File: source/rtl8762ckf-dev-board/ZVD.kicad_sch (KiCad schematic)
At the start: 4 parts, among them Q1 BC807DS,115, Q2 AO3401A

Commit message: implemented pico probe
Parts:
- Q1: footprint Package_SO:SC-74-6_1.5x2.9mm_P0.95mm -> Package_TO_SOT_SMD:SOT-363_SC-70-6; LCSC (none) -> C2836075; MPN (none) -> MMDT3906DW K3N
- Q2: LCSC (none) -> C15127; MPN (none) -> AO3401A
- R10: LCSC (none) -> C25792; MPN (none) -> 0402WGF4702TCE
- R9: LCSC (none) -> C25086; MPN (none) -> 0402WGF100KTCE
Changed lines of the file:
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@@
       (effects (font (size 1.27 1.27)) (justify left))
     )
-    (property "Footprint" "Package_SO:SC-74-6_1.5x2.9mm_P0.95mm" (at 48.26 58.42 0)
-      (effects (font (size 1.27 1.27)) hide)
-    )
-    (property "Datasheet" "http://www.diodes.com/_files/datasheets/ds30125.pdf" (at 53.34 60.96 0)
+    (property "Footprint" "Package_TO_SOT_SMD:SOT-363_SC-70-6" (at 48.26 58.42 0)
+      (effects (font (size 1.27 1.27)) hide)
+    )
+    (property "Datasheet" "https://datasheet.lcsc.com/lcsc/2202131900_CBI-MMDT3906DW-K3N_C2836075.pdf" (at 53.34 60.96 0)
+      (effects (font (size 1.27 1.27)) hide)
+    )
+    (property "LCSC" "C2836075" (at 53.34 60.96 0)
+      (effects (font (size 1.27 1.27)) hide)
+    )
+    (property "MPN" "MMDT3906DW K3N" (at 53.34 60.96 0)
       (effects (font (size 1.27 1.27)) hide)
     )
@@
       (effects (font (size 1.27 1.27)) (justify left) hide)
     )
+    (property "LCSC" "C15127" (at 63.5 53.34 0)
+      (effects (font (size 1.27 1.27)) hide)
+    )
+    (property "MPN" "AO3401A" (at 63.5 53.34 0)
+      (effects (font (size 1.27 1.27)) hide)
+    )
     (pin "1")
     (pin "2")
@@
       (project "rtl8762ckf-dev-board"
         (path "/5477044b-5ae5-4ed6-bb7d-f5f3cc95a2d4/c23b56eb-ac59-4603-b11b-f6fc1d31d5c9"
-          (reference "#PWR014") (unit 1)
+          (reference "#PWR031") (unit 1)
         )
       )
@@
       (project "rtl8762ckf-dev-board"
         (path "/5477044b-5ae5-4ed6-bb7d-f5f3cc95a2d4/c23b56eb-ac59-4603-b11b-f6fc1d31d5c9"
-          (reference "#PWR015") (unit 1)
+          (reference "#PWR032") (unit 1)
         )
       )
@@
       (effects (font (size 1.27 1.27)) hide)
     )
+    (property "LCSC" "C25792" (at 76.2 73.66 0)
+      (effects (font (size 1.27 1.27)) hide)
+    )
+    (property "MPN" "0402WGF4702TCE" (at 76.2 73.66 0)
+      (effects (font (size 1.27 1.27)) hide)
+    )
     (pin "1")
     (pin "2")
@@
       (project "rtl8762ckf-dev-board"
         (path "/5477044b-5ae5-4ed6-bb7d-f5f3cc95a2d4/c23b56eb-ac59-4603-b11b-f6fc1d31d5c9"
-          (reference "R5") (unit 1)
+          (reference "R9") (unit 1)
         )
       )
@@
       (effects (font (size 1.27 1.27)) (justify left))
     )
-    (property "Footprint" "Package_SO:SC-74-6_1.5x2.9mm_P0.95mm" (at 78.74 58.42 0)
-      (effects (font (size 1.27 1.27)) hide)
-    )
-    (property "Datasheet" "http://www.diodes.com/_files/datasheets/ds30125.pdf" (at 73.66 60.96 0)
+    (property "Footprint" "Package_TO_SOT_SMD:SOT-363_SC-70-6" (at 78.74 58.42 0)
+      (effects (font (size 1.27 1.27)) hide)
+    )
+    (property "Datasheet" "https://datasheet.lcsc.com/lcsc/2202131900_CBI-MMDT3906DW-K3N_C2836075.pdf" (at 73.66 60.96 0)
+      (effects (font (size 1.27 1.27)) hide)
+    )
+    (property "LCSC" "C2836075" (at 73.66 60.96 0)
+      (effects (font (size 1.27 1.27)) hide)
+    )
+    (property "MPN" "MMDT3906DW K3N" (at 73.66 60.96 0)
       (effects (font (size 1.27 1.27)) hide)
     )
@@
       (effects (font (size 1.27 1.27)) hide)
     )
-    (property "Datasheet" "~" (at 50.8 73.66 0)
+    (property "Datasheet" "https://datasheet.lcsc.com/lcsc/2205311900_UNI-ROYAL-Uniroyal-Elec-0402WGF100KTCE_C25086.pdf" (at 50.8 73.66 0)
+      (effects (font (size 1.27 1.27)) hide)
+    )
+    (property "LCSC" "C25086" (at 50.8 73.66 0)
+      (effects (font (size 1.27 1.27)) hide)
+    )
+    (property "MPN" "0402WGF100KTCE" (at 50.8 73.66 0)
       (effects (font (size 1.27 1.27)) hide)
     )
@@
       (project "rtl8762ckf-dev-board"
         (path "/5477044b-5ae5-4ed6-bb7d-f5f3cc95a2d4/c23b56eb-ac59-4603-b11b-f6fc1d31d5c9"
-          (reference "R4") (unit 1)
-        )
-      )
+          (reference "R8") (unit 1)
+        )
+      )

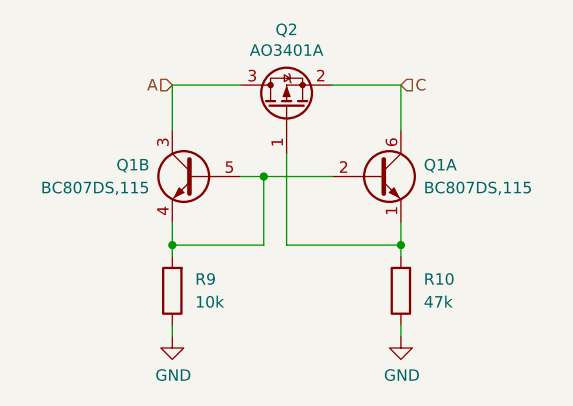
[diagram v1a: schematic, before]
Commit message: correct zvd; closes #4
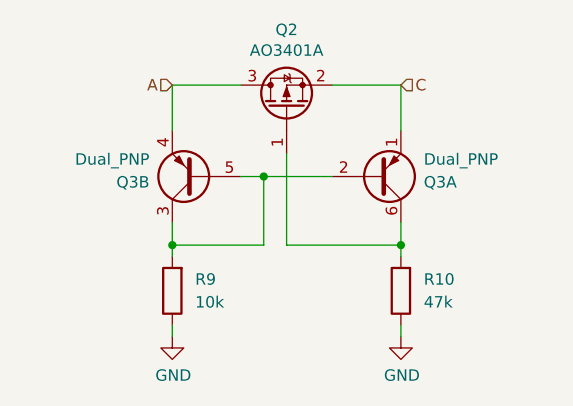
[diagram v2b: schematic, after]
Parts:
- removed Q1: BC807DS,115, Package_TO_SOT_SMD:SOT-363_SC-70-6, symbol Transistor_BJT:MMDT2222A
- added Q3: Dual_PNP, Package_TO_SOT_SMD:SOT-363_SC-70-6, symbol Device:Q_Dual_PNP_PNP_E1B1C2E2B2C1
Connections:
- net A: now also Q3.4 (E2)
- net C: now also Q3.1 (E1)
- net at R9.2: now also Q3.2 (B1), Q3.3 (C2), Q3.5 (B2)
- net at Q2.1 (G), R10.2: now also Q3.6 (C1)

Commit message: set correct PNs for R5, R8, R11; closes #5
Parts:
- R9: LCSC C25086 -> C25744; MPN 0402WGF100KTCE -> 0402WGF1002TCE
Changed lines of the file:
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@@
       (effects (font (size 1.27 1.27)) hide)
     )
-    (property "LCSC" "C25086" (at 50.8 73.66 0)
+    (property "LCSC" "C25744" (at 50.8 73.66 0)
       (effects (font (size 1.27 1.27)) hide)
     )
-    (property "MPN" "0402WGF100KTCE" (at 50.8 73.66 0)
+    (property "MPN" "0402WGF1002TCE" (at 50.8 73.66 0)
       (effects (font (size 1.27 1.27)) hide)
     )
